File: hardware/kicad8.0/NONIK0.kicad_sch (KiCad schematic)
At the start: 26 parts, among them J1 AVR-UPDI-3, J2 Qwiic/Stemma QT, J3 Test Pads, J4 Test Pads, Q1 S8050, SW1 SW_SPST, SW2 SW_Push, SW3 SW_Push, U1 LED_HCMS-2915, U2 ATtiny1604-SS, U3 AP3602A

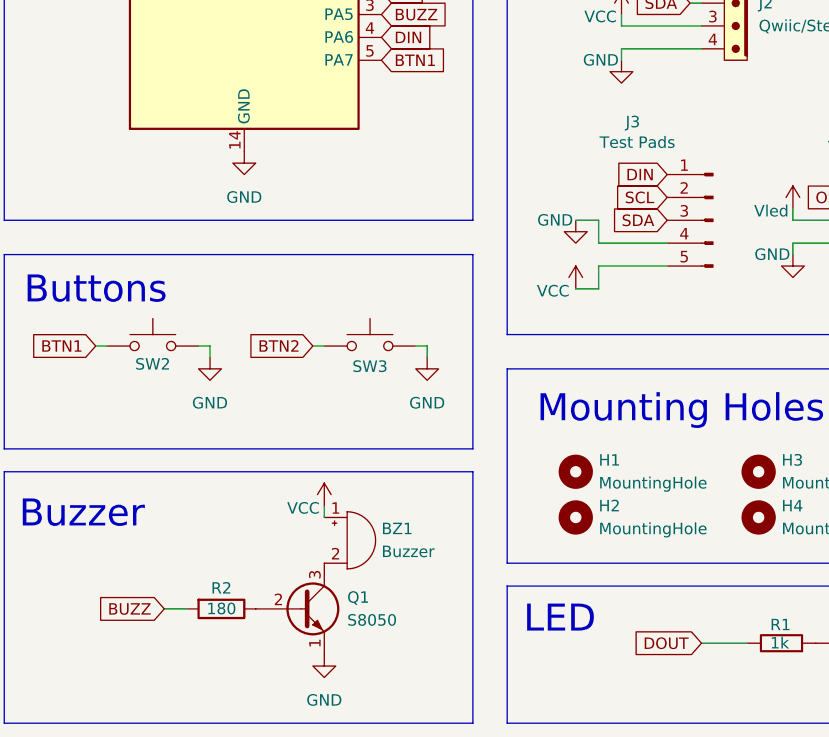
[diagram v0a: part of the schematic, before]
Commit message: adding flyback diode
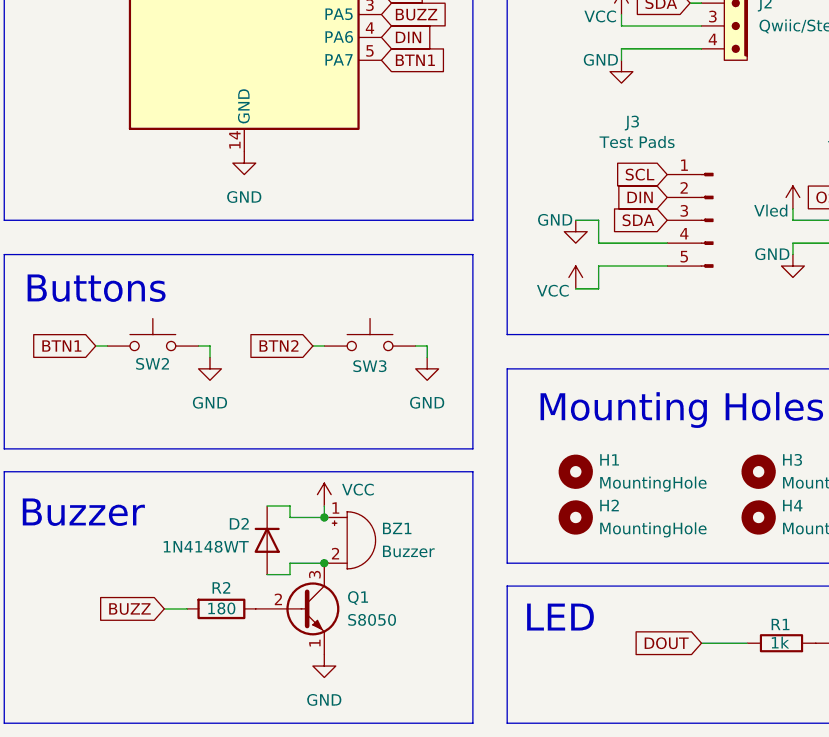
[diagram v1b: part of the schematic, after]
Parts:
- added D2: 1N4148WT, NONIK0:D_SOD-523_NoSilkscreen, symbol Diode:1N4148WT
- JP1: footprint NONIK0:SolderJumper-2_P1.3mm_Bridged_RoundedPad1.0x1.5mm -> NONIK0:SolderJumper_SmallerFootprint
- U3: footprint NONIK0:SOT-23-6 -> NONIK0:SOT-23-6_SmallerFootprint
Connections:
- net DIN: now also J3.2 (Pin_2); no longer J3.1 (Pin_1)
- net SCL: now also J3.1 (Pin_1); no longer J3.2 (Pin_2)
- net VCC: now also D2.1 (K)
- net at BZ1.2 (-), Q1.3 (C): now also D2.2 (A)
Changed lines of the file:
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@@
 	)
 	(junction
+		(at 115.57 105.41)
+		(diameter 0)
+		(color 0 0 0 0)
+	)
+	(junction
 		(at 58.42 132.08)
 		(diameter 0)
@@
 	)
 	(junction
+		(at 115.57 100.33)
+		(diameter 0)
+		(color 0 0 0 0)
+	)
+	(junction
 		(at 68.58 71.12)
 		(diameter 0)
@@
 	(wire
 		(pts
+			(xy 111.76 99.06) (xy 111.76 100.33)
+		)
+		(stroke
+			(width 0)
+			(type default)
+		)
+	)
+	(wire
+		(pts
 			(xy 31.75 135.89) (xy 33.02 135.89)
 		)
@@
 	(wire
 		(pts
+			(xy 111.76 106.68) (xy 111.76 105.41)
+		)
+		(stroke
+			(width 0)
+			(type default)
+		)
+	)
+	(wire
+		(pts
+			(xy 111.76 100.33) (xy 115.57 100.33)
+		)
+		(stroke
+			(width 0)
+			(type default)
+		)
+	)
+	(wire
+		(pts
 			(xy 148.59 45.72) (xy 148.59 44.45)
 		)
@@
 	(wire
 		(pts
+			(xy 111.76 105.41) (xy 115.57 105.41)
+		)
+		(stroke
+			(width 0)
+			(type default)
+		)
+	)
+	(wire
+		(pts
 			(xy 114.3 81.28) (xy 115.57 81.28)
 		)
@@
 	(wire
 		(pts
+			(xy 109.22 106.68) (xy 111.76 106.68)
+		)
+		(stroke
+			(width 0)
+			(type default)
+		)
+	)
+	(wire
+		(pts
 			(xy 31.75 140.97) (xy 33.02 140.97)
 		)
@@
 	(wire
 		(pts
+			(xy 109.22 99.06) (xy 111.76 99.06)
+		)
+		(stroke
+			(width 0)
+			(type default)
+		)
+	)
+	(wire
+		(pts
 			(xy 58.42 130.81) (xy 58.42 132.08)
 		)
@@
 		)
 	)
-	(global_label "DIN"
+	(global_label "SCL"
 		(shape input)
 		(at 153.67 62.23 180)
@@
 		)
 		(property "Intersheetrefs" "${INTERSHEET_REFS}"
-			(at 147.4795 62.23 0)
+			(at 147.1772 62.23 0)
 			(effects
 				(font
@@
 		)
 	)
+	(global_label "DIN"
+		(shape input)
+		(at 153.67 64.77 180)
+		(fields_autoplaced yes)
+		(effects
+			(font
+				(size 1.27 1.27)
+			)
+			(justify right)
+		)
+		(property "Intersheetrefs" "${INTERSHEET_REFS}"
+			(at 147.4795 64.77 0)
+			(effects
+				(font
+					(size 1.27 1.27)
+				)
+				(justify right)
+				(hide yes)
+			)
+		)
+	)
 	(global_label "BUZZ"
 		(shape input)
@@
 		)
 	)
-	(global_label "SCL"
-		(shape input)
-		(at 153.67 64.77 180)
-		(fields_autoplaced yes)
-		(effects
-			(font
-				(size 1.27 1.27)
-			)
-			(justify right)
-		)
-		(property "Intersheetrefs" "${INTERSHEET_REFS}"
-			(at 147.1772 64.77 0)
-			(effects
-				(font
-					(size 1.27 1.27)
-				)
-				(justify right)
-				(hide yes)
-			)
-		)
-	)
 	(global_label "DOUT"
 		(shape input)
@@
 		)
 		(property "Value" "VCC"
-			(at 115.062 99.314 0)
+			(at 121.158 97.282 0)
 			(effects
 				(font
@@
 			)
 		)
-		(property "Footprint" "NONIK0:SOT-23-6"
+		(property "Footprint" "NONIK0:SOT-23-6_SmallerFootprint"
 			(at 44.958 154.178 0)
 			(effects
@@
 			)
 		)
-		(property "Footprint" "NONIK0:SolderJumper-2_P1.3mm_Bridged_RoundedPad1.0x1.5mm"
+		(property "Footprint" "NONIK0:SolderJumper_SmallerFootprint"
 			(at 62.23 132.08 0)
 			(effects
@@
 					(unit 1)
 				)
+			)
+		)
+	)
+	(symbol
+		(lib_id "Diode:1N4148WT")
+		(at 109.22 102.87 270)
+		(unit 1)
+		(exclude_from_sim no)
+		(in_bom yes)
+		(on_board yes)
+		(dnp no)
+		(property "Reference" "D2"
+			(at 104.902 101.092 90)
+			(effects
+				(font
+					(size 1.27 1.27)
+				)
+				(justify left)
+			)
+		)
+		(property "Value" "1N4148WT"
+			(at 97.536 103.632 90)
+			(effects
+				(font
+					(size 1.27 1.27)
+				)
+				(justify left)
+			)
+		)
+		(property "Footprint" "NONIK0:D_SOD-523_NoSilkscreen"
+			(at 104.775 102.87 0)
+			(effects
+				(font
+					(size 1.27 1.27)
+				)
+				(hide yes)
+			)
+		)
+		(property "Datasheet" "https://www.diodes.com/assets/Datasheets/ds30396.pdf"
+			(at 109.22 102.87 0)
+			(effects
+				(font
+					(size 1.27 1.27)
+				)
+				(hide yes)
+			)
+		)
+		(property "Description" "75V 0.15A Fast switching Diode, SOD-523"
+			(at 109.22 102.87 0)
+			(effects
+				(font
+					(size 1.27 1.27)
+				)
+				(hide yes)
+			)
+		)
+		(property "Sim.Device" "D"
+			(at 109.22 102.87 0)
+			(effects
+				(font
+					(size 1.27 1.27)
+				)
+				(hide yes)
+			)
+		)
+		(property "Sim.Pins" "1=K 2=A"
+			(at 109.22 102.87 0)
+			(effects
+				(font
+					(size 1.27 1.27)
+				)
+				(hide yes)
+			)
+		)
+		(pin "1"
+		)
+		(pin "2"
+		)
+		(instances
+			(project ""
+				(path "/1b540e36-998f-4dd7-90ae-747ee59fea59"
+					(reference "D2")
+					(unit 1)
+				)
